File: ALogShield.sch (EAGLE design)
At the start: 32 parts, among them U1 DS3231MZ/V+T

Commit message: Symmetry with screw terminals and buttons
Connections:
- removed net N$1: A0.2, C15D.1
- removed net N$2: A1.2, C15C.1
- removed net N$3: A2.2, C15B.1
- removed net N$4: A3.2, C15A.1
- net A0: now also A0.2, C15D.1
- net A1: now also A1.2, C15C.1
- net A2: now also A2.2, C15B.1
- net A3: now also A3.2, C15A.1
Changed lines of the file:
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@@
 <pinref part="H2" gate="G$1" pin="5"/>
+</segment>
+<segment>
+<pinref part="A2" gate="G$1" pin="2"/>
+<pinref part="C15" gate="B" pin="1"/>
+<wire x1="35.56" y1="-185.42" x2="45.72" y2="-185.42" width="0.1524" layer="91"/>
+<label x="38.1" y="-185.42" size="1.778" layer="95"/>
 </segment>
 </net>
@@
 <pinref part="H2" gate="G$1" pin="1"/>
 </segment>
+<segment>
+<pinref part="A0" gate="G$1" pin="2"/>
+<pinref part="C15" gate="D" pin="1"/>
+<wire x1="35.56" y1="-165.1" x2="45.72" y2="-165.1" width="0.1524" layer="91"/>
+<label x="38.1" y="-165.1" size="1.778" layer="95"/>
+</segment>
 </net>
 <net name="A3" class="0">
@@
 <label x="45.72" y="-129.54" size="1.778" layer="95"/>
 <pinref part="H2" gate="G$1" pin="7"/>
+</segment>
+<segment>
+<pinref part="C15" gate="A" pin="1"/>
+<pinref part="A3" gate="G$1" pin="2"/>
+<wire x1="45.72" y1="-195.58" x2="35.56" y2="-195.58" width="0.1524" layer="91"/>
+<label x="38.1" y="-195.58" size="1.778" layer="95"/>
 </segment>
 </net>
@@
 <pinref part="H2" gate="G$1" pin="3"/>
 </segment>
+<segment>
+<pinref part="A1" gate="G$1" pin="2"/>
+<pinref part="C15" gate="C" pin="1"/>
+<wire x1="35.56" y1="-175.26" x2="45.72" y2="-175.26" width="0.1524" layer="91"/>
+<label x="38.1" y="-175.26" size="1.778" layer="95"/>
+</segment>
 </net>
 <net name="CS-SD" class="0">
@@
 </segment>
 </net>
-<net name="N$1" class="0">
-<segment>
-<pinref part="A0" gate="G$1" pin="2"/>
-<pinref part="C15" gate="D" pin="1"/>
-<wire x1="35.56" y1="-165.1" x2="45.72" y2="-165.1" width="0.1524" layer="91"/>
-</segment>
-</net>
-<net name="N$2" class="0">
-<segment>
-<pinref part="A1" gate="G$1" pin="2"/>
-<pinref part="C15" gate="C" pin="1"/>
-<wire x1="35.56" y1="-175.26" x2="45.72" y2="-175.26" width="0.1524" layer="91"/>
-</segment>
-</net>
-<net name="N$3" class="0">
-<segment>
-<pinref part="A2" gate="G$1" pin="2"/>
-<pinref part="C15" gate="B" pin="1"/>
-<wire x1="35.56" y1="-185.42" x2="45.72" y2="-185.42" width="0.1524" layer="91"/>
-</segment>
-</net>
-<net name="N$4" class="0">
-<segment>
-<pinref part="C15" gate="A" pin="1"/>
-<pinref part="A3" gate="G$1" pin="2"/>
-<wire x1="45.72" y1="-195.58" x2="35.56" y2="-195.58" width="0.1524" layer="91"/>
-</segment>
-</net>

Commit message: Bye bye, ISP header and reset cap and R
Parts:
- removed COUT1: 0.1uF, rcl:C-EUC0603
- removed ISP1: AVRISP-6, adafruit:AVRISP-6
- removed R_RESET: 10k, rcl:R-US_R0603
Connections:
- removed net DTR: COUT1.1
- net CLK: no longer ISP1.SCK
- net DI: no longer ISP1.MOSI
- net DO: no longer ISP1.MISO
- net GND: no longer ISP1.GND
- net RESET: no longer COUT1.2, ISP1.RST, R_RESET.1
- net VCC: no longer ISP1.VCC, R_RESET.2
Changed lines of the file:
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@@
 <part name="SD1" library="adafruit" deviceset="SDMMC" device="06132"/>
 <part name="CLOCK_BATT1" library="SparkFun" deviceset="BATTERY" device="12PTH" value="3V Backup Battery"/>
-<part name="R_RESET" library="rcl" deviceset="R-US_" device="R0603" value="10k"/>
-<part name="P+1" library="supply1" deviceset="VCC" device=""/>
 <part name="SUPPLY31" library="supply2" deviceset="GND" device=""/>
 <part name="A0" library="resistor" deviceset="R-US_" device="0207/10"/>
@@
 <part name="A3" library="resistor" deviceset="R-US_" device="0207/10"/>
 <part name="SUPPLY34" library="supply2" deviceset="GND" device=""/>
-<part name="ISP1" library="adafruit" deviceset="AVRISP" device="-6"/>
-<part name="P+4" library="supply1" deviceset="VCC" device=""/>
-<part name="SUPPLY35" library="supply2" deviceset="GND" device=""/>
 <part name="SUPPLY36" library="supply2" deviceset="GND" device=""/>
 <part name="SUPPLY41" library="supply2" deviceset="GND" device=""/>
@@
 <part name="CLOCK_BATT_DECOUP" library="rcl" deviceset="C-EU" device="C0603" value="0.1uF"/>
 <part name="SUPPLY56" library="supply2" deviceset="GND" device=""/>
-<part name="COUT1" library="rcl" deviceset="C-EU" device="C0603" value="0.1uF"/>
 <part name="D2" library="semicon-smd-ipc" deviceset="DIODE_AC-CA_" device="" value="BAT54"/>
 <part name="LOG" library="SparkFun-Electromechanical" deviceset="SWITCH-MOMENTARY-2" device="PTH" value="LOG"/>
@@
 <instance part="SD1" gate="G$1" x="271.78" y="-287.02"/>
 <instance part="CLOCK_BATT1" gate="G$1" x="137.16" y="-416.56" rot="R270"/>
-<instance part="R_RESET" gate="G$1" x="157.48" y="-167.64" rot="R90"/>
-<instance part="P+1" gate="VCC" x="157.48" y="-154.94"/>
 <instance part="SUPPLY31" gate="GND" x="157.48" y="-195.58"/>
 <instance part="A0" gate="G$1" x="30.48" y="-165.1"/>
@@
 <instance part="A3" gate="G$1" x="30.48" y="-195.58"/>
 <instance part="SUPPLY34" gate="GND" x="337.82" y="-307.34"/>
-<instance part="ISP1" gate="G$1" x="48.26" y="-360.68"/>
-<instance part="P+4" gate="VCC" x="73.66" y="-358.14" rot="R270"/>
-<instance part="SUPPLY35" gate="GND" x="71.12" y="-365.76"/>
 <instance part="SUPPLY36" gate="GND" x="93.98" y="-434.34"/>
 <instance part="SUPPLY41" gate="GND" x="251.46" y="-271.78"/>
@@
 </instance>
 <instance part="SUPPLY56" gate="GND" x="137.16" y="-426.72"/>
-<instance part="COUT1" gate="G$1" x="142.24" y="-175.26" rot="R90"/>
 <instance part="D2" gate="G$1" x="109.22" y="-160.02" rot="R180"/>
 <instance part="LOG" gate="G$1" x="109.22" y="-177.8" rot="R90"/>
@@
 </segment>
 <segment>
-<wire x1="157.48" y1="-157.48" x2="157.48" y2="-162.56" width="0.1524" layer="91"/>
-<pinref part="R_RESET" gate="G$1" pin="2"/>
-<pinref part="P+1" gate="VCC" pin="VCC"/>
-</segment>
-<segment>
-<wire x1="63.5" y1="-358.14" x2="71.12" y2="-358.14" width="0.1524" layer="91"/>
-<label x="66.04" y="-358.14" size="1.778" layer="95"/>
-<pinref part="ISP1" gate="G$1" pin="VCC"/>
-<pinref part="P+4" gate="VCC" pin="VCC"/>
-</segment>
-<segment>
 <label x="116.84" y="-121.92" size="1.778" layer="95"/>
 <wire x1="111.76" y1="-121.92" x2="129.54" y2="-121.92" width="0.1524" layer="91"/>
@@
 </segment>
 <segment>
-<wire x1="63.5" y1="-360.68" x2="71.12" y2="-360.68" width="0.1524" layer="91"/>
-<label x="66.04" y="-360.68" size="1.778" layer="95"/>
-<pinref part="ISP1" gate="G$1" pin="MOSI"/>
-</segment>
-<segment>
 <wire x1="129.54" y1="-119.38" x2="116.84" y2="-119.38" width="0.1524" layer="91"/>
 <label x="116.84" y="-119.38" size="1.778" layer="95"/>
@@
 </segment>
 <segment>
-<wire x1="35.56" y1="-358.14" x2="27.94" y2="-358.14" width="0.1524" layer="91"/>
-<label x="27.94" y="-358.14" size="1.778" layer="95"/>
-<pinref part="ISP1" gate="G$1" pin="MISO"/>
-</segment>
-<segment>
 <wire x1="129.54" y1="-116.84" x2="116.84" y2="-116.84" width="0.1524" layer="91"/>
 <label x="116.84" y="-116.84" size="1.778" layer="95"/>
@@
 <label x="210.82" y="-289.56" size="1.778" layer="95"/>
 <pinref part="LSHIFT1" gate="A" pin="I"/>
-</segment>
-<segment>
-<wire x1="35.56" y1="-360.68" x2="27.94" y2="-360.68" width="0.1524" layer="91"/>
-<label x="27.94" y="-360.68" size="1.778" layer="95"/>
-<pinref part="ISP1" gate="G$1" pin="SCK"/>
 </segment>
 <segment>
@@
 <pinref part="LSHIFT1" gate="D" pin="I"/>
 <pinref part="SUPPLY34" gate="GND" pin="GND"/>
-</segment>
-<segment>
-<wire x1="63.5" y1="-363.22" x2="71.12" y2="-363.22" width="0.1524" layer="91"/>
-<label x="66.04" y="-363.22" size="1.778" layer="95"/>
-<pinref part="ISP1" gate="G$1" pin="GND"/>
-<pinref part="SUPPLY35" gate="GND" pin="GND"/>
 </segment>
 <segment>
@@
 </segment>
 <segment>
-<wire x1="157.48" y1="-175.26" x2="157.48" y2="-172.72" width="0.1524" layer="91"/>
 <wire x1="157.48" y1="-175.26" x2="157.48" y2="-177.8" width="0.1524" layer="91"/>
 <wire x1="157.48" y1="-175.26" x2="170.18" y2="-175.26" width="0.1524" layer="91"/>
-<wire x1="147.32" y1="-175.26" x2="157.48" y2="-175.26" width="0.1524" layer="91"/>
-<junction x="157.48" y="-175.26"/>
 <label x="162.56" y="-175.26" size="1.778" layer="95"/>
-<pinref part="R_RESET" gate="G$1" pin="1"/>
 <pinref part="RESET" gate="G$1" pin="2"/>
-<pinref part="COUT1" gate="G$1" pin="2"/>
-</segment>
-<segment>
-<wire x1="27.94" y1="-363.22" x2="35.56" y2="-363.22" width="0.1524" layer="91"/>
-<label x="27.94" y="-363.22" size="1.778" layer="95"/>
-<pinref part="ISP1" gate="G$1" pin="RST"/>
 </segment>
 </net>
@@
 </segment>
 </net>
-<net name="DTR" class="0">
-<segment>
-<wire x1="139.7" y1="-175.26" x2="127" y2="-175.26" width="0.1524" layer="91"/>
-<label x="127" y="-175.26" size="1.778" layer="95"/>
-<pinref part="COUT1" gate="G$1" pin="1"/>
-</segment>
-</net>

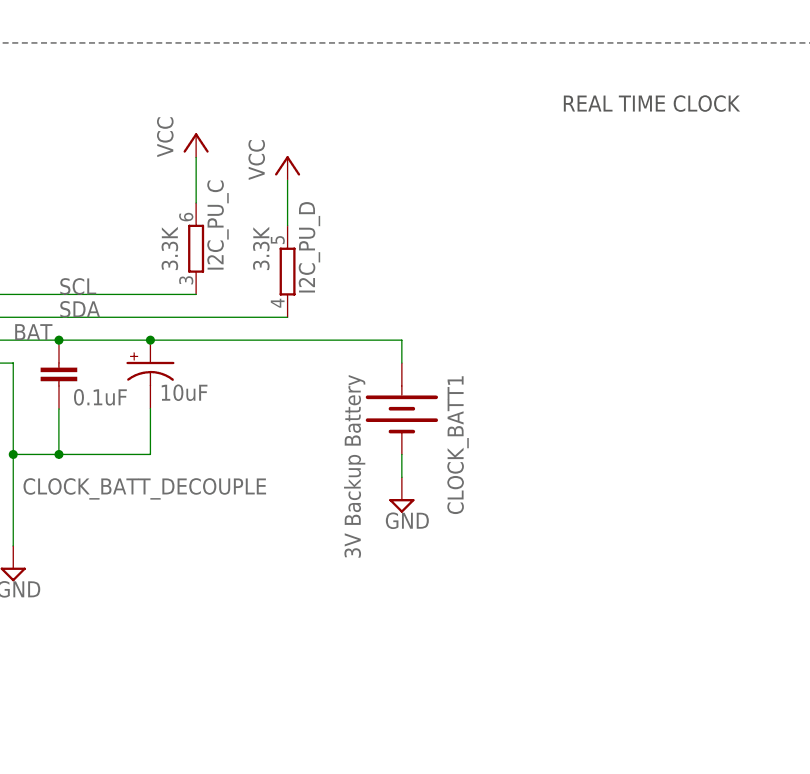
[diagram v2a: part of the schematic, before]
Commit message: SMD battery clip
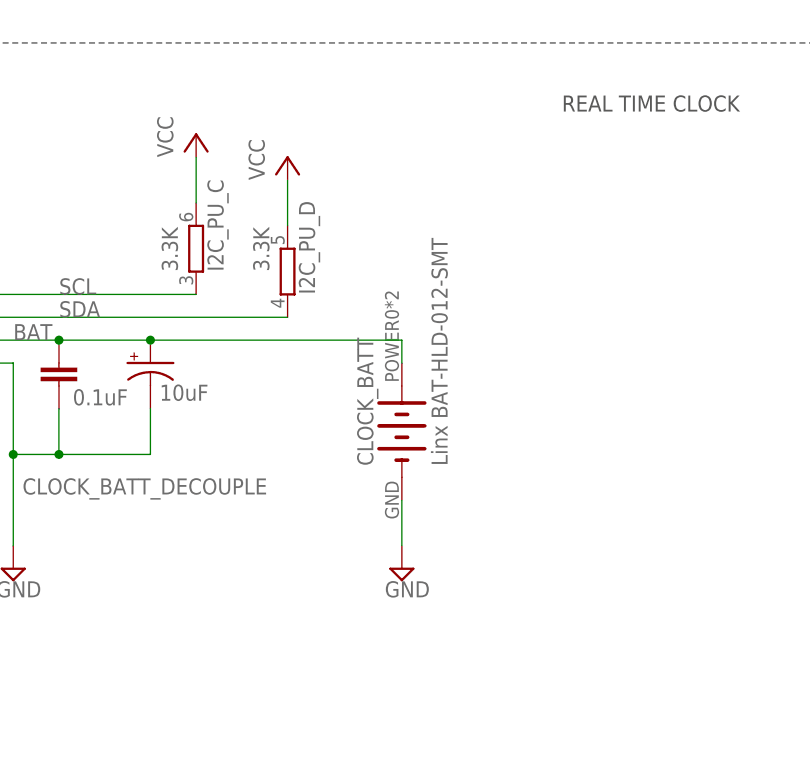
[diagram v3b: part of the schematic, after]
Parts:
- removed CLOCK_BATT1: 3V Backup Battery, SparkFun:BATTERY12PTH
- added CLOCK_BATT: Linx BAT-HLD-012-SMT, awickert:LINX-BAT-HLD-012-SMT-OTL
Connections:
- net BAT: now also CLOCK_BATT.+; no longer CLOCK_BATT1.+
- net GND: now also CLOCK_BATT.-; no longer CLOCK_BATT1.-
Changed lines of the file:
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@@
 <part name="SUPPLY26" library="supply2" deviceset="GND" device=""/>
 <part name="SD1" library="adafruit" deviceset="SDMMC" device="06132"/>
-<part name="CLOCK_BATT1" library="SparkFun" deviceset="BATTERY" device="12PTH" value="3V Backup Battery"/>
 <part name="SUPPLY31" library="supply2" deviceset="GND" device=""/>
 <part name="A0" library="resistor" deviceset="R-US_" device="0207/10"/>
@@
 <part name="3V1" library="csandell" deviceset="MIC5380_LARGE_PADS" device=""/>
 <part name="C15" library="rc-master-smd" deviceset="CCA_" device="" value="10nF"/>
+<part name="CLOCK_BATT" library="awickert" deviceset="LINX-BAT-HLD-012-SMT-OTL" device="" value="Linx BAT-HLD-012-SMT"/>
 </parts>
 <sheets>
@@
 <instance part="SUPPLY26" gate="GND" x="340.36" y="-292.1"/>
 <instance part="SD1" gate="G$1" x="271.78" y="-287.02"/>
-<instance part="CLOCK_BATT1" gate="G$1" x="137.16" y="-416.56" rot="R270"/>
 <instance part="SUPPLY31" gate="GND" x="157.48" y="-195.58"/>
 <instance part="A0" gate="G$1" x="30.48" y="-165.1"/>
@@
 <attribute name="VALUE" x="100.584" y="-416.179" size="1.778" layer="96"/>
 </instance>
-<instance part="SUPPLY56" gate="GND" x="137.16" y="-426.72"/>
+<instance part="SUPPLY56" gate="GND" x="137.16" y="-434.34"/>
 <instance part="D2" gate="G$1" x="109.22" y="-160.02" rot="R180"/>
 <instance part="LOG" gate="G$1" x="109.22" y="-177.8" rot="R90"/>
@@
 <instance part="C15" gate="C" x="48.26" y="-175.26"/>
 <instance part="C15" gate="D" x="48.26" y="-165.1"/>
+<instance part="CLOCK_BATT" gate="G$1" x="137.16" y="-419.1" rot="R90"/>
 </instances>
 <busses>
@@
 </segment>
 <segment>
-<pinref part="CLOCK_BATT1" gate="G$1" pin="-"/>
 <pinref part="SUPPLY56" gate="GND" pin="GND"/>
-<wire x1="137.16" y1="-424.18" x2="137.16" y2="-421.64" width="0.1524" layer="91"/>
+<wire x1="137.16" y1="-431.8" x2="137.16" y2="-426.72" width="0.1524" layer="91"/>
+<pinref part="CLOCK_BATT" gate="G$1" pin="-"/>
 </segment>
 <segment>
@@
 <junction x="109.22" y="-408.94"/>
 <pinref part="U1" gate="A" pin="VBAT"/>
-<pinref part="CLOCK_BATT1" gate="G$1" pin="+"/>
 <wire x1="137.16" y1="-408.94" x2="137.16" y2="-411.48" width="0.1524" layer="91"/>
-</segment>
-</net>
+<pinref part="CLOCK_BATT" gate="G$1" pin="+"/>
+</segment>
+</net>
